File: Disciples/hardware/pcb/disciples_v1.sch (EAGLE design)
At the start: 118 parts, among them IC1 OPA1641, IC2 LM324PW, IC3 LM324PW, IC4 TL072D, IC5 LM324PW, IC6 LM4040B10, IC7 LM4040B50, IC8 LM324PW, IC9 LM324PW, J1 PJ301_THONKICONN6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

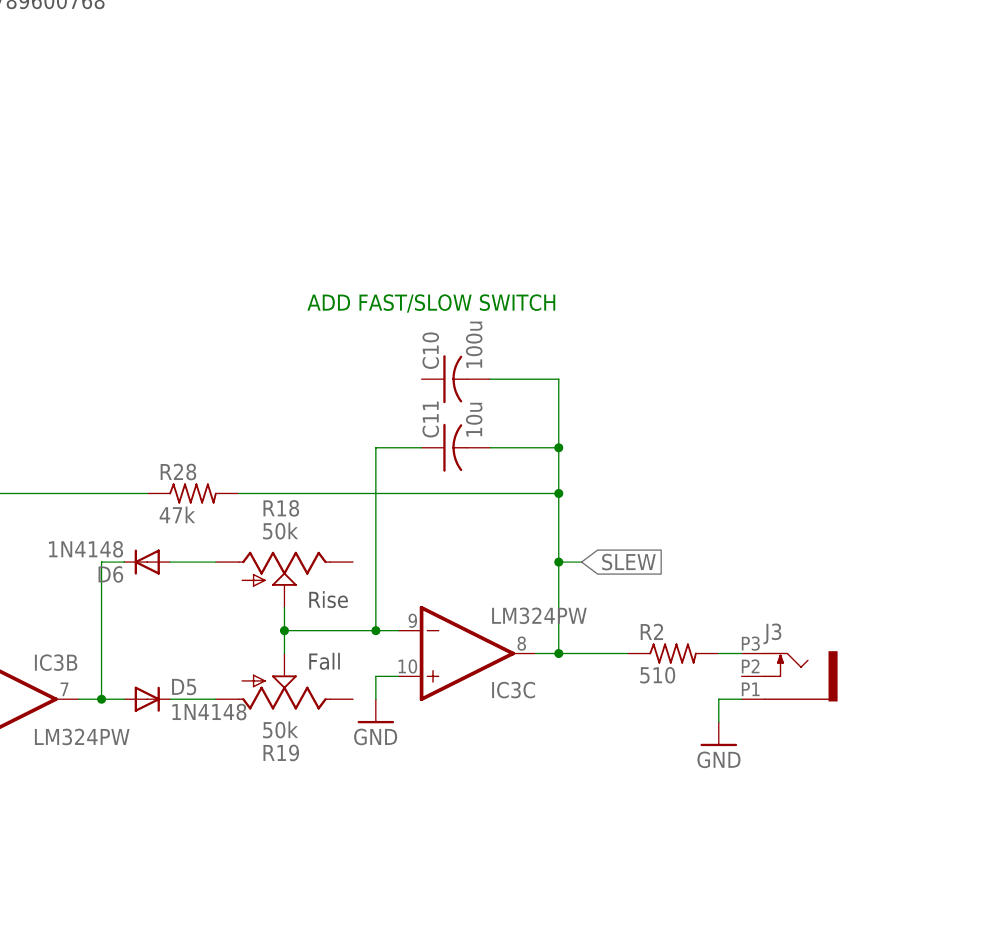
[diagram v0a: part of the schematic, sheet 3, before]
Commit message: Added stability resistor
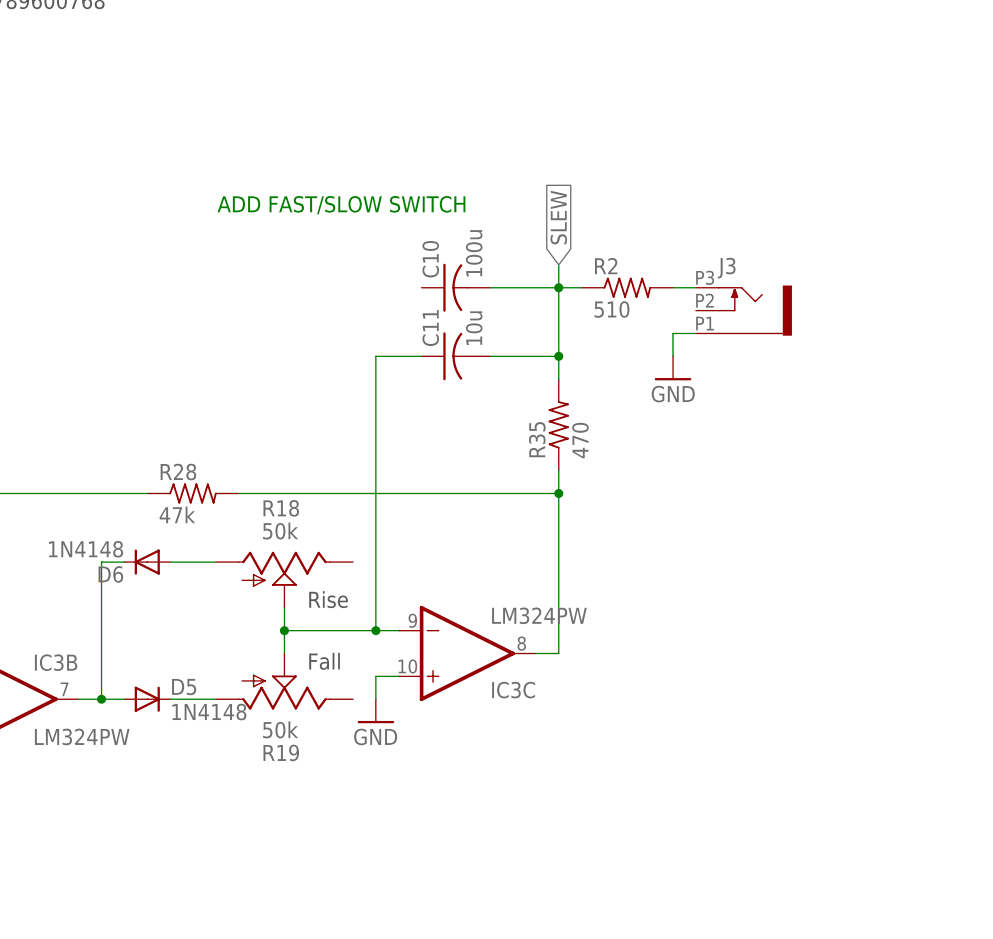
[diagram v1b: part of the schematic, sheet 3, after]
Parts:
- added R35: 470, rcl:R-US_R0402
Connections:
- new net N$55: IC3C.OUT, R28.2, R35.1
- net SLEW: now also R35.2; no longer IC3C.OUT, R28.2
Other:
- moved on the sheet: C10, C11, J3, R2
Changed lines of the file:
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@@
 <part name="C25" library="rcl" deviceset="C-US" device="C0402" value="100n"/>
 <part name="C26" library="rcl" deviceset="C-US" device="C0402" value="100n"/>
+<part name="R35" library="rcl" deviceset="R-US_" device="R0402" value="470"/>
 </parts>
 <sheets>
@@
 <text x="121.92" y="38.1" size="1.778" layer="97">Slew Level</text>
 <text x="180.34" y="99.06" size="1.778" layer="97">Rise</text>
-<text x="180.34" y="132.08" size="1.778" layer="91">ADD FAST/SLOW SWITCH</text>
+<text x="198.12" y="144.78" size="1.778" layer="91" rot="R180">ADD FAST/SLOW SWITCH</text>
 </plain>
 <instances>
@@
 <attribute name="NAME" x="25.4" y="95.504" size="1.778" layer="95" rot="MR0"/>
 </instance>
-<instance part="GND15" gate="1" x="226.06" y="83.82" smashed="yes" rot="MR0">
-<attribute name="VALUE" x="228.6" y="81.28" size="1.778" layer="96" rot="MR0"/>
-</instance>
-<instance part="J3" gate="G$1" x="233.68" y="91.44" smashed="yes">
-<attribute name="NAME" x="231.14" y="95.504" size="1.778" layer="95"/>
-</instance>
-<instance part="R2" gate="G$1" x="220.98" y="93.98" smashed="yes">
-<attribute name="NAME" x="217.17" y="95.4786" size="1.778" layer="95"/>
-<attribute name="VALUE" x="217.17" y="90.678" size="1.778" layer="96"/>
+<instance part="GND15" gate="1" x="220.98" y="124.46" smashed="yes" rot="MR0">
+<attribute name="VALUE" x="223.52" y="121.92" size="1.778" layer="96" rot="MR0"/>
+</instance>
+<instance part="J3" gate="G$1" x="228.6" y="132.08" smashed="yes">
+<attribute name="NAME" x="226.06" y="136.144" size="1.778" layer="95"/>
+</instance>
+<instance part="R2" gate="G$1" x="215.9" y="134.62" smashed="yes">
+<attribute name="NAME" x="212.09" y="136.1186" size="1.778" layer="95"/>
+<attribute name="VALUE" x="212.09" y="131.318" size="1.778" layer="96"/>
 </instance>
 <instance part="D5" gate="G$1" x="162.56" y="88.9" smashed="yes">
@@
 <attribute name="VALUE" x="90.17" y="90.678" size="1.778" layer="96"/>
 </instance>
-<instance part="C11" gate="G$1" x="195.58" y="116.84" smashed="yes" rot="R90">
-<attribute name="NAME" x="194.945" y="117.856" size="1.778" layer="95" rot="R90"/>
-<attribute name="VALUE" x="199.771" y="117.856" size="1.778" layer="96" rot="R90"/>
+<instance part="C11" gate="G$1" x="195.58" y="127" smashed="yes" rot="R90">
+<attribute name="NAME" x="194.945" y="128.016" size="1.778" layer="95" rot="R90"/>
+<attribute name="VALUE" x="199.771" y="128.016" size="1.778" layer="96" rot="R90"/>
 </instance>
 <instance part="GND6" gate="1" x="101.6" y="83.82" smashed="yes">
@@
 <attribute name="VALUE" x="105.41" y="29.718" size="1.778" layer="96"/>
 </instance>
-<instance part="C10" gate="G$1" x="195.58" y="124.46" smashed="yes" rot="R90">
-<attribute name="NAME" x="194.945" y="125.476" size="1.778" layer="95" rot="R90"/>
-<attribute name="VALUE" x="199.771" y="125.476" size="1.778" layer="96" rot="R90"/>
+<instance part="C10" gate="G$1" x="195.58" y="134.62" smashed="yes" rot="R90">
+<attribute name="NAME" x="194.945" y="135.636" size="1.778" layer="95" rot="R90"/>
+<attribute name="VALUE" x="199.771" y="135.636" size="1.778" layer="96" rot="R90"/>
+</instance>
+<instance part="R35" gate="G$1" x="208.28" y="119.38" smashed="yes" rot="R90">
+<attribute name="NAME" x="206.7814" y="115.57" size="1.778" layer="95" rot="R90"/>
+<attribute name="VALUE" x="211.582" y="115.57" size="1.778" layer="96" rot="R90"/>
 </instance>
 </instances>
@@
 </segment>
 <segment>
-<wire x1="228.6" y1="88.9" x2="226.06" y2="88.9" width="0.1524" layer="91"/>
-<wire x1="226.06" y1="88.9" x2="226.06" y2="86.36" width="0.1524" layer="91"/>
+<wire x1="223.52" y1="129.54" x2="220.98" y2="129.54" width="0.1524" layer="91"/>
+<wire x1="220.98" y1="129.54" x2="220.98" y2="127" width="0.1524" layer="91"/>
 <pinref part="J3" gate="G$1" pin="1"/>
 <pinref part="GND15" gate="1" pin="GND"/>
@@
 <net name="N$16" class="0">
 <segment>
-<wire x1="226.06" y1="93.98" x2="228.6" y2="93.98" width="0.1524" layer="91"/>
+<wire x1="220.98" y1="134.62" x2="223.52" y2="134.62" width="0.1524" layer="91"/>
 <pinref part="R2" gate="G$1" pin="2"/>
 <pinref part="J3" gate="G$1" pin="3"/>
@@
 </net>
 <net name="SLEW" class="0">
-<segment>
-<wire x1="208.28" y1="93.98" x2="208.28" y2="104.14" width="0.1524" layer="91"/>
-<pinref part="R28" gate="G$1" pin="2"/>
-<wire x1="208.28" y1="104.14" x2="208.28" y2="111.76" width="0.1524" layer="91"/>
-<wire x1="208.28" y1="111.76" x2="172.72" y2="111.76" width="0.1524" layer="91"/>
-<junction x="208.28" y="104.14"/>
-<pinref part="R2" gate="G$1" pin="1"/>
-<label x="210.82" y="104.14" size="1.778" layer="95" xref="yes"/>
-<wire x1="208.28" y1="93.98" x2="215.9" y2="93.98" width="0.1524" layer="91"/>
-<wire x1="210.82" y1="104.14" x2="208.28" y2="104.14" width="0.1524" layer="91"/>
-<pinref part="IC3" gate="C" pin="OUT"/>
-<wire x1="208.28" y1="93.98" x2="205.74" y2="93.98" width="0.1524" layer="91"/>
-<junction x="208.28" y="93.98"/>
-<pinref part="C11" gate="G$1" pin="2"/>
-<wire x1="200.66" y1="116.84" x2="208.28" y2="116.84" width="0.1524" layer="91"/>
-<wire x1="208.28" y1="116.84" x2="208.28" y2="111.76" width="0.1524" layer="91"/>
-<junction x="208.28" y="111.76"/>
-<pinref part="C10" gate="G$1" pin="2"/>
-<wire x1="200.66" y1="124.46" x2="208.28" y2="124.46" width="0.1524" layer="91"/>
-<wire x1="208.28" y1="124.46" x2="208.28" y2="116.84" width="0.1524" layer="91"/>
-<junction x="208.28" y="116.84"/>
-</segment>
 <segment>
 <label x="116.84" y="17.78" size="1.778" layer="95" rot="R180" xref="yes"/>
 <wire x1="116.84" y1="17.78" x2="119.38" y2="17.78" width="0.1524" layer="91"/>
 <pinref part="IC5" gate="A" pin="+IN"/>
+</segment>
+<segment>
+<pinref part="C10" gate="G$1" pin="2"/>
+<wire x1="200.66" y1="134.62" x2="208.28" y2="134.62" width="0.1524" layer="91"/>
+<wire x1="208.28" y1="134.62" x2="208.28" y2="127" width="0.1524" layer="91"/>
+<pinref part="C11" gate="G$1" pin="2"/>
+<wire x1="200.66" y1="127" x2="208.28" y2="127" width="0.1524" layer="91"/>
+<pinref part="R35" gate="G$1" pin="2"/>
+<wire x1="208.28" y1="124.46" x2="208.28" y2="127" width="0.1524" layer="91"/>
+<junction x="208.28" y="127"/>
+<pinref part="R2" gate="G$1" pin="1"/>
+<wire x1="208.28" y1="134.62" x2="210.82" y2="134.62" width="0.1524" layer="91"/>
+<junction x="208.28" y="134.62"/>
+<wire x1="208.28" y1="134.62" x2="208.28" y2="137.16" width="0.1524" layer="91"/>
+<label x="208.28" y="137.16" size="1.778" layer="95" rot="R90" xref="yes"/>
 </segment>
 </net>
@@
 <junction x="187.96" y="96.52"/>
 <pinref part="C11" gate="G$1" pin="1"/>
-<wire x1="193.04" y1="116.84" x2="187.96" y2="116.84" width="0.1524" layer="91"/>
-<wire x1="187.96" y1="116.84" x2="187.96" y2="96.52" width="0.1524" layer="91"/>
+<wire x1="193.04" y1="127" x2="187.96" y2="127" width="0.1524" layer="91"/>
+<wire x1="187.96" y1="127" x2="187.96" y2="96.52" width="0.1524" layer="91"/>
 </segment>
 </net>
@@
 </segment>
 </net>
+<net name="N$55" class="0">
+<segment>
+<pinref part="R28" gate="G$1" pin="2"/>
+<wire x1="172.72" y1="111.76" x2="208.28" y2="111.76" width="0.1524" layer="91"/>
+<wire x1="208.28" y1="111.76" x2="208.28" y2="93.98" width="0.1524" layer="91"/>
+<pinref part="IC3" gate="C" pin="OUT"/>
+<wire x1="208.28" y1="93.98" x2="205.74" y2="93.98" width="0.1524" layer="91"/>
+<pinref part="R35" gate="G$1" pin="1"/>
+<wire x1="208.28" y1="111.76" x2="208.28" y2="114.3" width="0.1524" layer="91"/>
+<junction x="208.28" y="111.76"/>
+</segment>
+</net>

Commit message: Forgot a wire
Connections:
- net GND: now also R24.E
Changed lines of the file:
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@@
 <wire x1="139.7" y1="78.74" x2="142.24" y2="78.74" width="0.1524" layer="91"/>
+</segment>
+<segment>
+<pinref part="GND34" gate="1" pin="GND"/>
+<pinref part="R24" gate="G$1" pin="E"/>
+<wire x1="101.6" y1="76.2" x2="101.6" y2="78.74" width="0.1524" layer="91"/>
 </segment>
 </net>
